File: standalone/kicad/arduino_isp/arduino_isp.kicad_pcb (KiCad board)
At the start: 2 copper layers, 10 parts, among them J1 ICSP, J2 ICSP, J3 Conn_01x09, J4 Conn_01x06

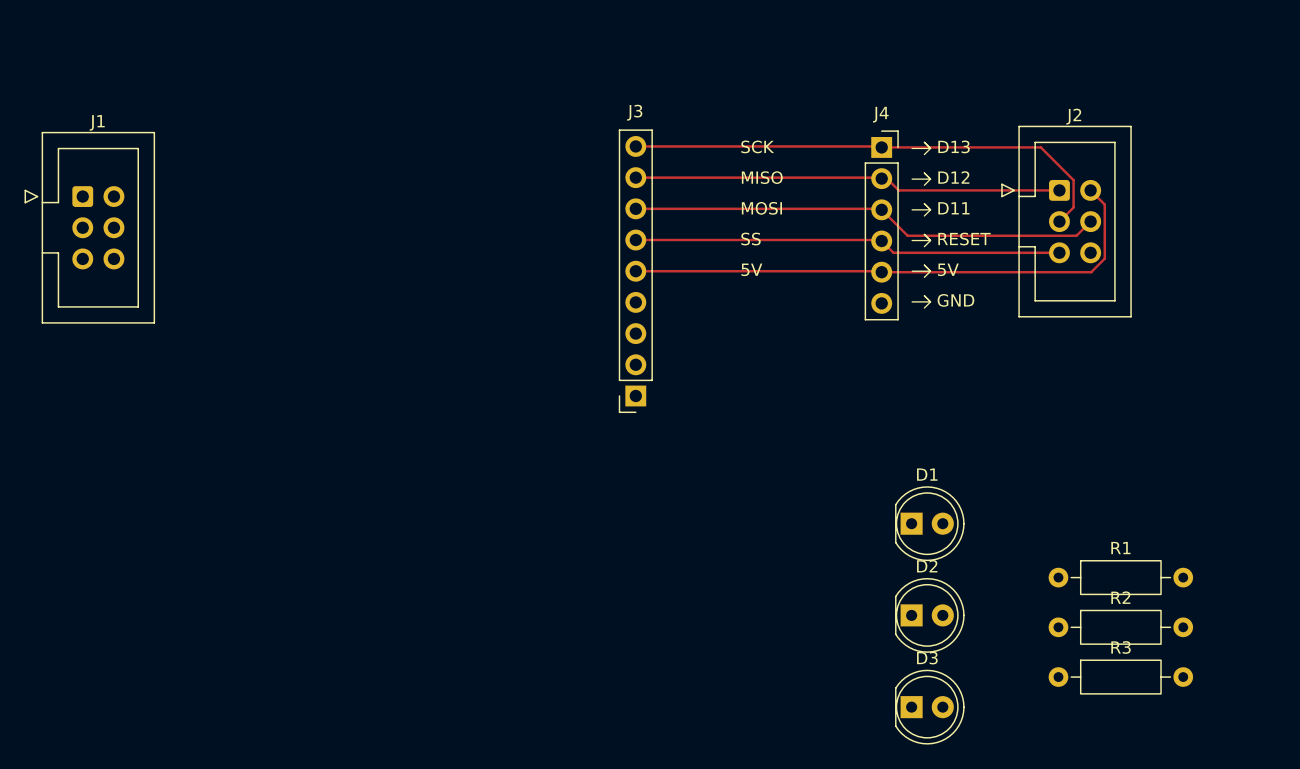
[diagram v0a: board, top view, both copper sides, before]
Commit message: PCB do Arduino ISP
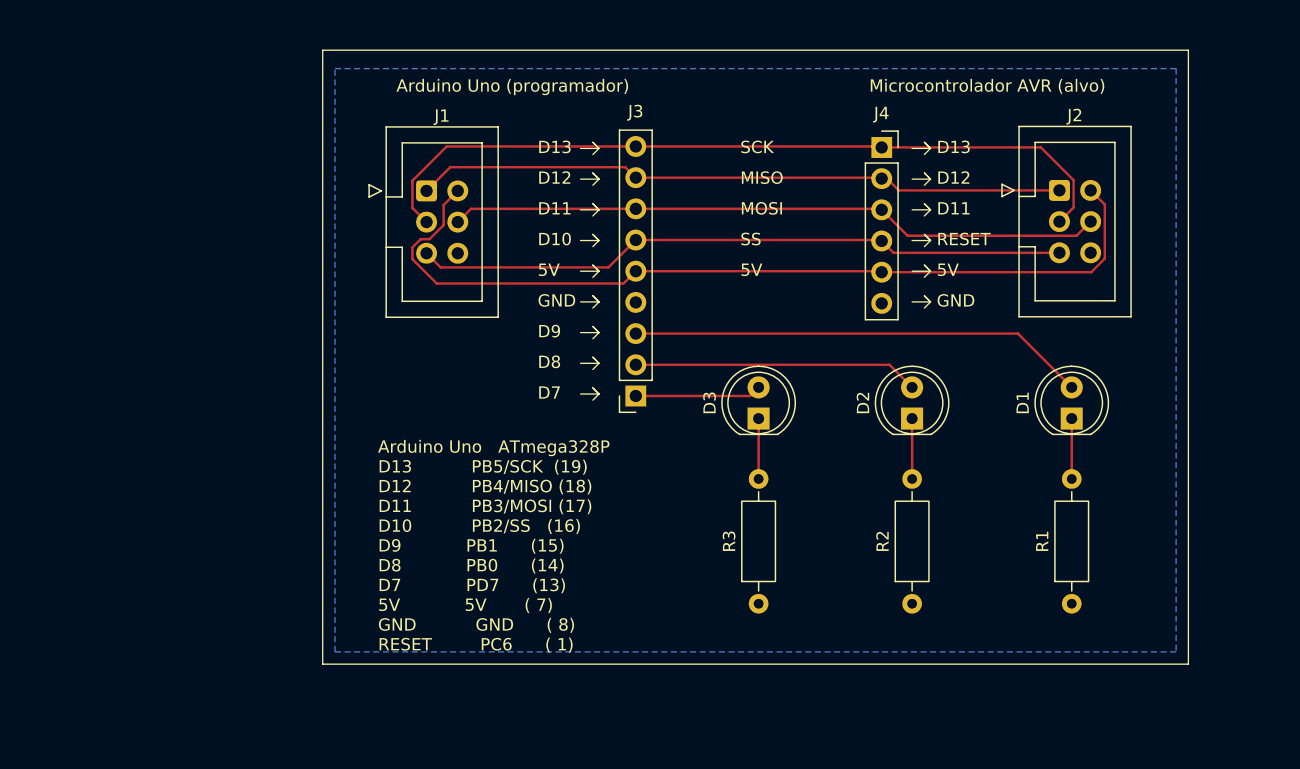
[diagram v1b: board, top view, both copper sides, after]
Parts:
- moved J1 28.0 mm to (90.5, 50.5)
- moved D3 26.6 mm to (117.5, 69.0), turned to 90 degrees
- moved R3 25.1 mm to (117.5, 84.1), turned to 90 degrees
- moved D2 16.0 mm to (130.0, 69.0), turned to 90 degrees
- moved D1 15.6 mm to (143.0, 69.0), turned to 90 degrees
- moved R2 12.1 mm to (130.0, 84.1), turned to 90 degrees
- moved R1 2.39 mm to (143.0, 84.1), turned to 90 degrees
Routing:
- net Net-(D1-A): track 0.00 -> 37.3 mm
- net +5V: track 44.7 -> 71.6 mm
- net Net-(D2-A): track 0.00 -> 23.3 mm
- net /SCK: track 40.6 -> 63.8 mm
- net /SS: track 34.9 -> 53.4 mm
- net /MISO: track 34.9 -> 53.1 mm
- net /MOSI: track 38.4 -> 53.4 mm
- net Net-(D3-A): track 0.00 -> 10.3 mm
- net Net-(D3-K): track 0.00 -> 4.92 mm
- net Net-(D2-K): track 0.00 -> 4.92 mm
- net Net-(D1-K): track 0.00 -> 4.92 mm
- added copper zone on B.Cu, net GND
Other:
- board text added: "Arduino Uno (programador)"
- board text added: "Arduino Uno ATmega328P D13 PB5/SCK (19) D12 PB4/MISO (18) D11 PB3/MOSI (17) D10 PB2/SS (16) D9 PB1 (15) D8 PB0 (14) D7 PD7 (13) 5V 5V ( 7) GND GND ( 8) RESET PC6 ( 1)"
- board text added: "D10"
- board text added: "D7"
- board text added: "D8"
- board text added: "D9"
- board text added: "Microcontrolador AVR (alvo)"

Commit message: Atualizações na placa
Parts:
- removed J2: ICSP, Connector_IDC:IDC-Header_2x03_P2.54mm_Vertical
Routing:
- net +5V: track 71.6 -> 47.0 mm
- net /SCK: track 63.8 -> 43.3 mm
- net /MOSI: track 53.4 -> 35.0 mm
- net /SS: track 53.4 -> 38.5 mm
- net /MISO: track 53.1 -> 38.7 mm
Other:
- board outline added: 70.5 x 50 mm
- board text added: "5V ( 7)"
- board text added: "GND ( 8)"
- board text added: "PB3/MOSI (17)"
- board text added: "PB4/MISO (18)"
- board text added: "PB5/SCK (19)"
- board text added: "PC6/RESET ( 1)"
- board text removed: "Arduino Uno ATmega328P D13 PB5/SCK (19) D12 PB4/MISO (18) D11 PB3/MOSI (17) D10 PB2/SS (16) D9 PB1 (15) D8 PB0 (14) D7 PD7 (13) 5V 5V ( 7) GND GND ( 8) RESET PC6 ( 1)"
- board text removed: "RESET"

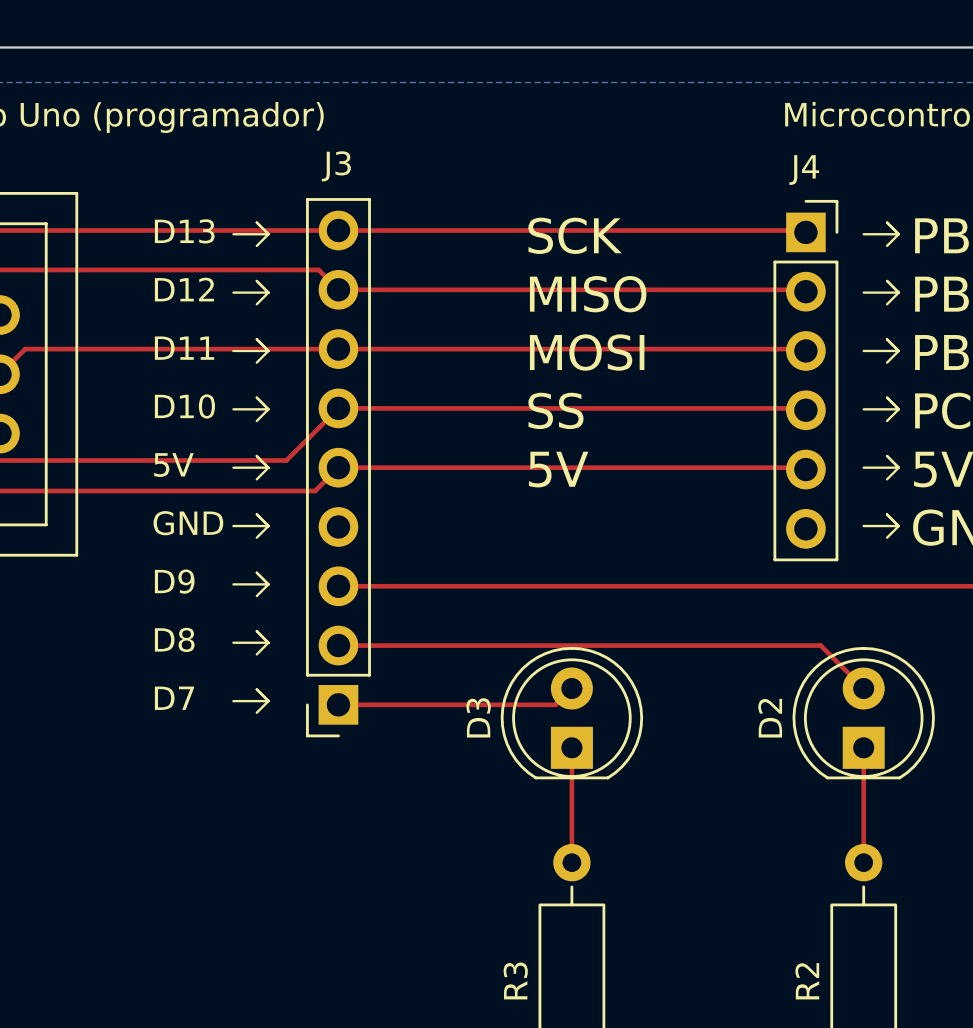
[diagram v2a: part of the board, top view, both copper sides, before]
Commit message: Troca do conector de 9 para 10 pinos
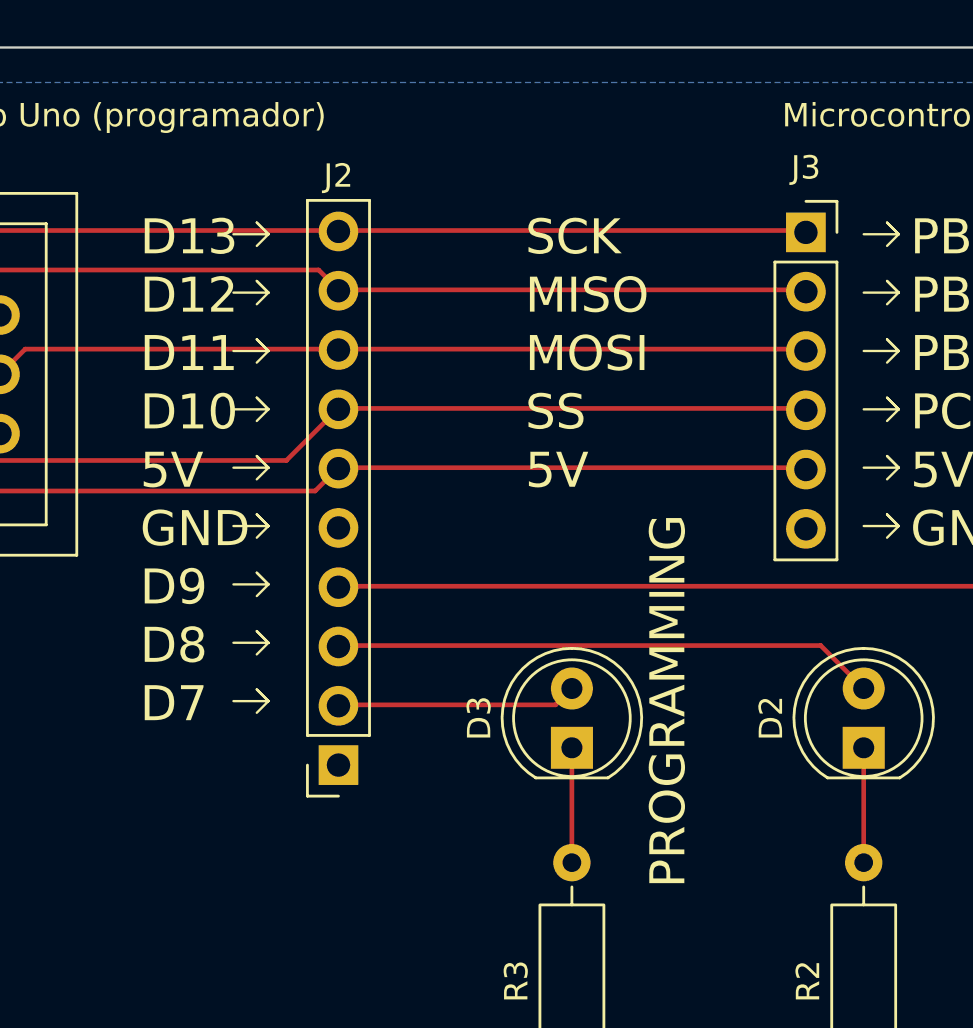
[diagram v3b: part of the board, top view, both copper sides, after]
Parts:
- removed the J3 at (107.5, 67.2)
- added J2: Conn_01x10, Connector_PinSocket_2.54mm:PinSocket_1x10_P2.54mm_Vertical, F.Cu at (107.5, 69.7)
- renumbered J4 to J3
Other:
- board text added: "PROGRAMMING"

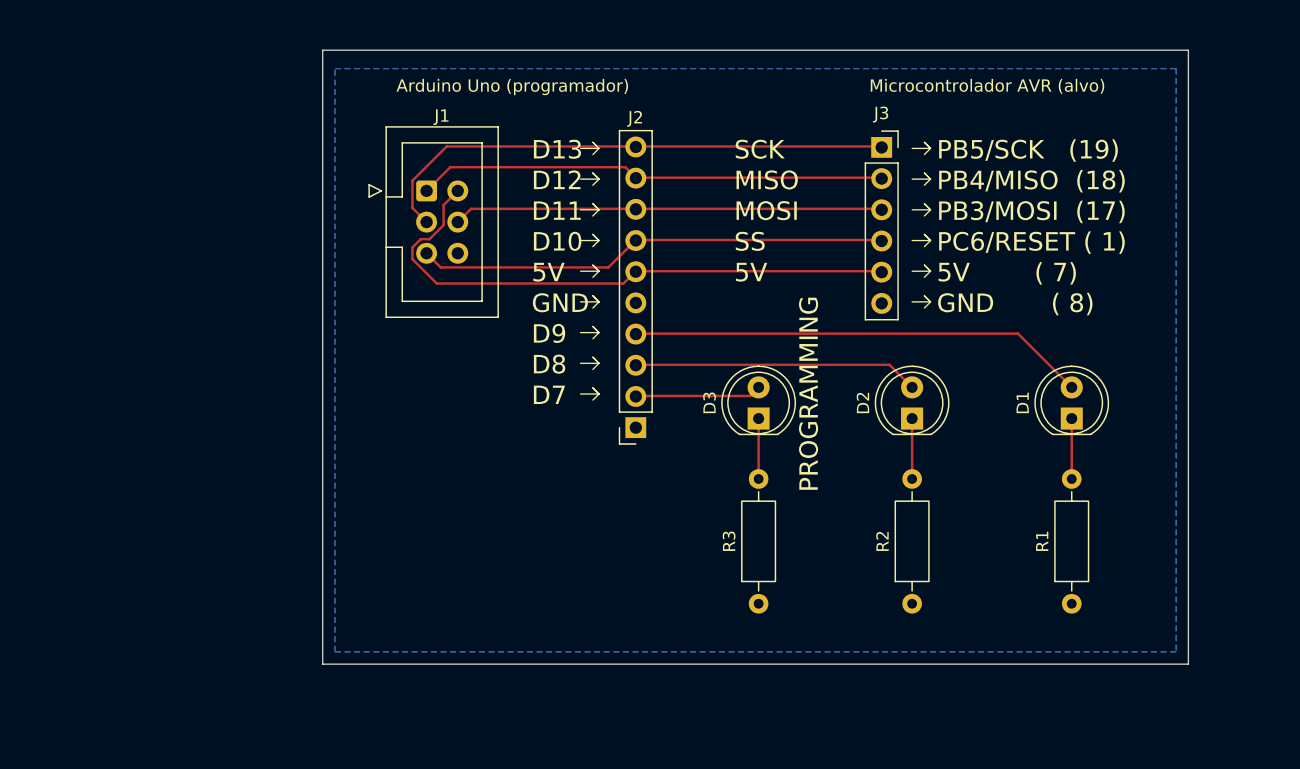
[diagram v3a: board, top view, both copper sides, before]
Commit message: Ajustes no Silkscreen
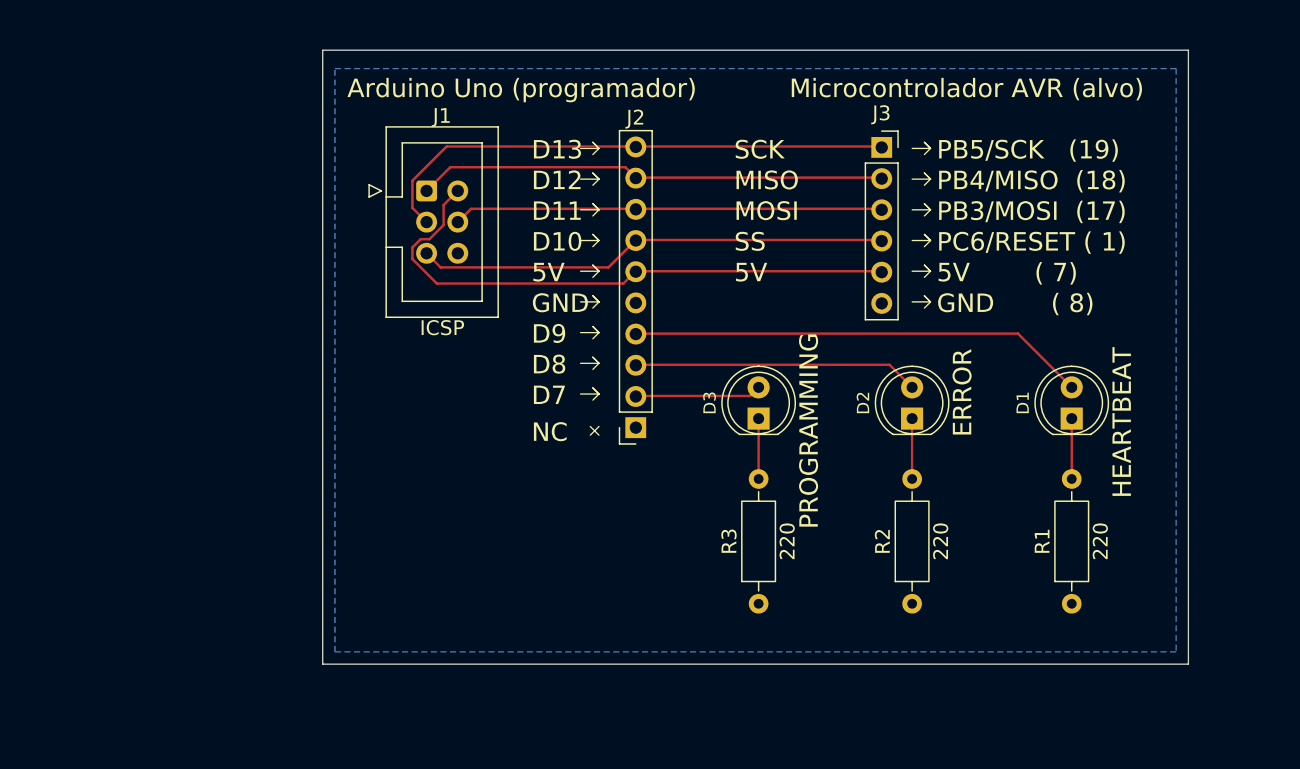
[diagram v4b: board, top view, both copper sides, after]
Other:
- board text added: "ERROR"
- board text added: "HEARTBEAT"
- board text added: "NC"

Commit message: Finalização da placa Aruino ISP
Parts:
- removed the J1 at (90.5, 50.5)
- added G***: LOGO, logo_computacao_raiz:logo_computacao_raiz_20x11mm, F.Cu at (98.0, 80.0)
- moved J1 10.5 mm to (97.0, 70.2)
- moved D3 4.53 mm to (113.0, 69.5)
- moved R3 4.53 mm to (113.0, 84.6)
- moved D2 2.06 mm to (128.0, 69.5)
- moved R2 2.06 mm to (128.0, 84.6)
- moved D1 0.50 mm to (143.0, 69.5)
- moved J2 0.50 mm to (127.5, 47.4)
- moved R1 0.50 mm to (143.0, 84.6)
- renumbered J2 to J1, J3 to J2
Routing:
- net +5V: track 47.0 -> 30.6 mm
- net /SCK: track 43.3 -> 30.6 mm
- net Net-(D1-A): track 37.3 -> 47.8 mm
- net Net-(D2-A): track 23.3 -> 31.7 mm
- net /SS: track 38.5 -> 30.6 mm
- net /MISO: track 38.7 -> 31.0 mm
- net Net-(D3-A): track 10.3 -> 16.3 mm
- net /MOSI: track 35.0 -> 30.6 mm
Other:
- board text added: "μControlador AVR alvo (ATmega48/88/168/328 DIP)"
- board text removed: "Microcontrolador AVR (alvo)"
